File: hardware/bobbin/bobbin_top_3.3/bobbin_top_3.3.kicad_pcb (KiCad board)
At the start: 2 copper layers, 68.5 x 8.5 mm, 1 part

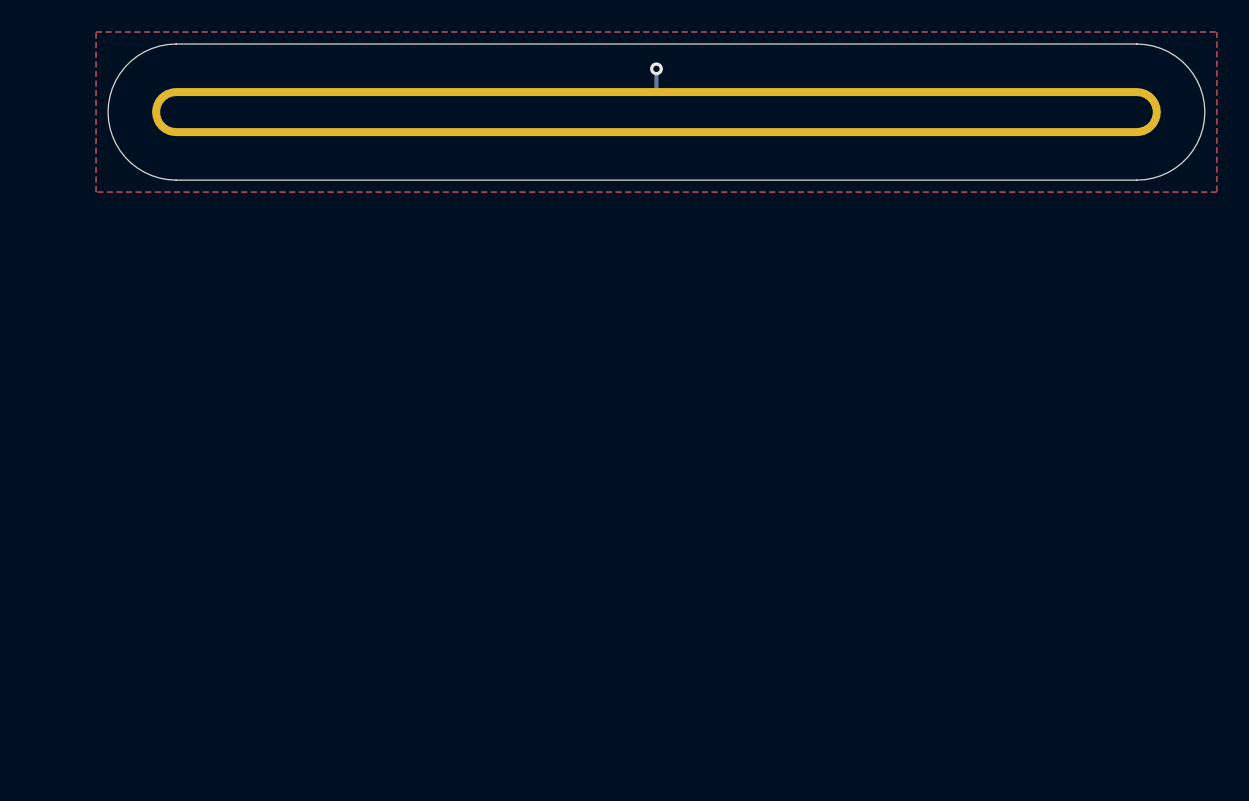
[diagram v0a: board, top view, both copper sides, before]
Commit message: Copied over bobbin_bottom to bobbin_top
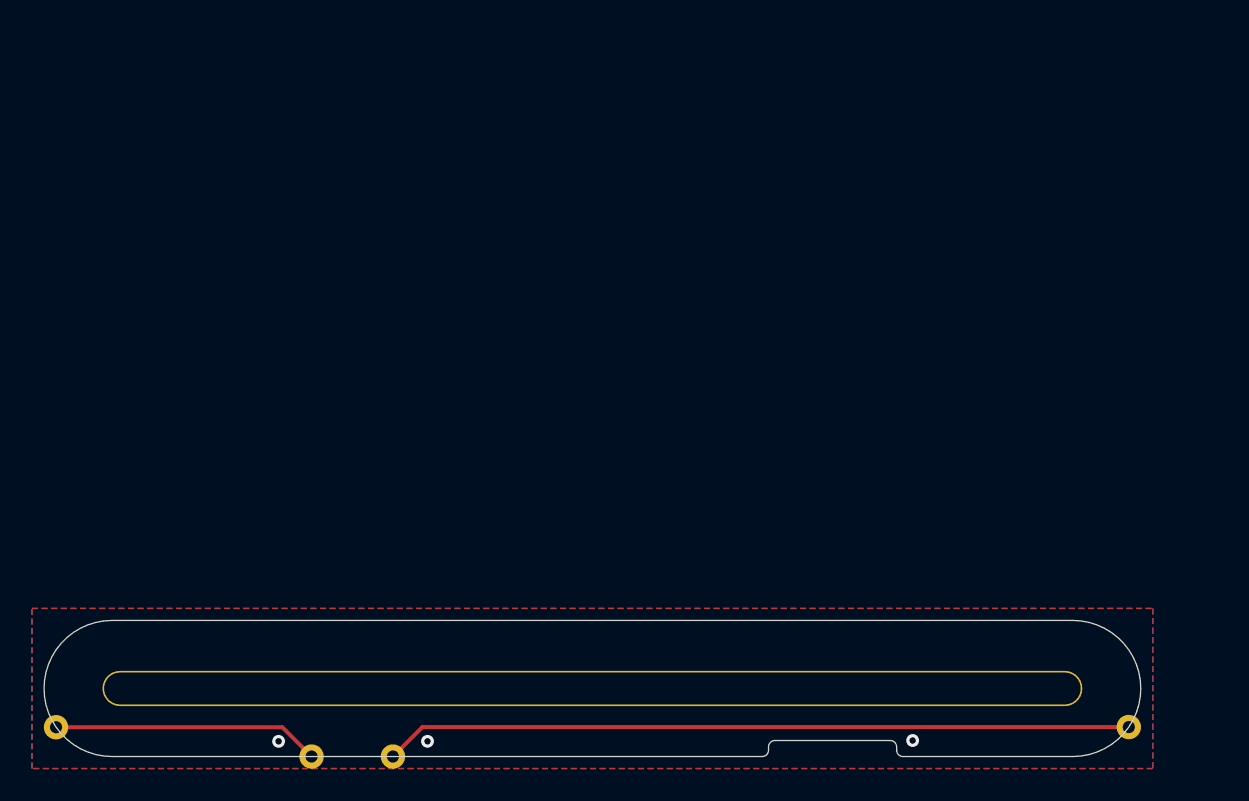
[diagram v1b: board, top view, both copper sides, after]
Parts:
- removed H3: ground-pad, cycfi_library:xr2-3.3-bobbin-top
- added H1: single_pad, xr_spectra_library:rail_slot_3.3, F.Cu at (130.0, 101.0)
- added J1: OC, cycfi_library:single-pad-1.52x1.52-th, F.Cu at (117.5, 105.2)
- added J2: OC, cycfi_library:single-pad-1.52x1.52-th, F.Cu at (163.5, 103.4)
- added J3: IC, cycfi_library:single-pad-1.52x1.52-th, F.Cu at (96.5, 103.4)
- added J4: IC, cycfi_library:single-pad-1.52x1.52-th, F.Cu at (112.5, 105.2)
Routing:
- net /OC: track 0.00 -> 46.7 mm
- net /IC: track 0.00 -> 16.7 mm
- net GND: track 2.70 -> 0.00 mm, vias 1 -> 3
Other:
- outline, holes or cut-outs redrawn
- net class Default removed

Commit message: Bobbin-top done
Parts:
- removed J1, J2: OC, cycfi_library:single-pad-1.52x1.52-th
- removed J3, J4: IC, cycfi_library:single-pad-1.52x1.52-th
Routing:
- net /OC: track 46.7 -> 0.00 mm
- net /IC: track 16.7 -> 0.00 mm
- net GND: vias 3 -> 0
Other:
- outline, holes or cut-outs redrawn
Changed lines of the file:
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@@
   (net 0 "")
   (net 1 "GND")
-  (net 2 "/OC")
-  (net 3 "/IC")
-  (footprint "cycfi_library:single-pad-1.52x1.52-th" (layer "F.Cu")
-    (at 117.54 105.25 180)
-    (property "Sheetfile" "bobbin_bottom_3.3.kicad_sch")
-    (property "Sheetname" "")
-    (attr through_hole)
-    (fp_text reference "J1" (at 0 2.54 180) (layer "F.SilkS") hide
-      (effects (font (size 1 1) (thickness 0.15)))
-    )
-    (fp_text value "OC" (at 0 -2.54 180) (layer "F.Fab")
-      (effects (font (size 1 1) (thickness 0.15)))
-    )
-    (pad "1" thru_hole circle (at 0 0 180) (size 1.52 1.52) (drill 0.76) (layers *.Cu *.Mask)
-      (net 2 "/OC") (pinfunction "Pin_1") (pintype "passive"))
-  )
-  (footprint "cycfi_library:single-pad-1.52x1.52-th" (layer "F.Cu")
-    (at 163.5 103.41 180)
-    (property "Sheetfile" "bobbin_bottom_3.3.kicad_sch")
-    (property "Sheetname" "")
-    (attr through_hole)
-    (fp_text reference "J2" (at 0 2.54) (layer "F.SilkS") hide
-      (effects (font (size 1 1) (thickness 0.15)))
-    )
-    (fp_text value "OC" (at -3 -0.09) (layer "F.Fab")
-      (effects (font (size 1 1) (thickness 0.15)))
-    )
-    (pad "1" thru_hole circle (at 0 0 180) (size 1.52 1.52) (drill 0.76) (layers *.Cu *.Mask)
-      (net 2 "/OC") (pinfunction "Pin_1") (pintype "passive"))
-  )
-  (footprint "cycfi_library:single-pad-1.52x1.52-th" (layer "F.Cu")
-    (at 96.5 103.42)
-    (property "Sheetfile" "bobbin_bottom_3.3.kicad_sch")
-    (property "Sheetname" "")
-    (attr through_hole)
-    (fp_text reference "J3" (at 0 2.54) (layer "F.SilkS") hide
-      (effects (font (size 1 1) (thickness 0.15)))
-    )
-    (fp_text value "IC" (at -2.75 0.08) (layer "F.Fab")
-      (effects (font (size 1 1) (thickness 0.15)))
-    )
-    (pad "1" thru_hole circle (at 0 0) (size 1.52 1.52) (drill 0.76) (layers *.Cu *.Mask)
-      (net 3 "/IC") (pinfunction "Pin_1") (pintype "passive"))
-  )
   (footprint "xr_spectra_library:rail_slot_3.3" (layer "F.Cu")
     (at 130 101)
-    (property "Sheetfile" "bobbin_bottom_3.3.kicad_sch")
+    (property "Sheetfile" "bobbin_top_3.3.kicad_sch")
     (property "Sheetname" "")
     (attr through_hole)
@@
     (pad "1" thru_hole oval (at 0 0) (size 61.2 2.2) (drill oval 61 2) (layers *.Cu *.Mask)
       (net 1 "GND") (pinfunction "1") (pintype "input"))
-  )
-  (footprint "cycfi_library:single-pad-1.52x1.52-th" (layer "F.Cu")
-    (at 112.46 105.25)
-    (property "Sheetfile" "bobbin_bottom_3.3.kicad_sch")
-    (property "Sheetname" "")
-    (attr through_hole)
-    (fp_text reference "J4" (at 0 2.54) (layer "F.SilkS") hide
-      (effects (font (size 1 1) (thickness 0.15)))
-    )
-    (fp_text value "IC" (at 0 2.25) (layer "F.Fab")
-      (effects (font (size 1 1) (thickness 0.15)))
-    )
-    (pad "1" thru_hole circle (at 0 0) (size 1.52 1.52) (drill 0.76) (layers *.Cu *.Mask)
-      (net 3 "/IC") (pinfunction "Pin_1") (pintype "passive"))
   )
   (gr_arc (start 149.4 105.25) (mid 149.117157 105.132843) (end 149 104.85) (layer "Dwgs.User") (width 0.01))
@@
   (gr_arc (start 100 105.25) (mid 95.75 101) (end 100 96.75) (layer "Dwgs.User") (width 0.01))
   (gr_line (start 141.4 104.25) (end 148.6 104.25) (layer "Dwgs.User") (width 0.01))
-  (gr_arc (start 148.6 104.25) (mid 148.882843 104.367157) (end 149 104.65) (layer "Edge.Cuts") (width 0.01))
-  (gr_line (start 141 104.85) (end 141 104.65) (layer "Edge.Cuts") (width 0.01))
-  (gr_line (start 149 104.65) (end 149 104.85) (layer "Edge.Cuts") (width 0.01))
-  (gr_arc (start 141 104.85) (mid 140.882843 105.132843) (end 140.6 105.25) (layer "Edge.Cuts") (width 0.01))
-  (gr_arc (start 141 104.65) (mid 141.117157 104.367157) (end 141.4 104.25) (layer "Edge.Cuts") (width 0.01))
   (gr_line (start 100 96.75) (end 160 96.75) (layer "Edge.Cuts") (width 0.01))
   (gr_arc (start 100 105.25) (mid 95.75 101) (end 100 96.75) (layer "Edge.Cuts") (width 0.01))
-  (gr_line (start 141.4 104.25) (end 148.6 104.25) (layer "Edge.Cuts") (width 0.01))
-  (gr_arc (start 149.4 105.25) (mid 149.117157 105.132843) (end 149 104.85) (layer "Edge.Cuts") (width 0.01))
-  (gr_line (start 140.6 105.25) (end 100 105.25) (layer "Edge.Cuts") (width 0.01))
-  (gr_line (start 160 105.25) (end 149.4 105.25) (layer "Edge.Cuts") (width 0.01))
+  (gr_line (start 160 105.25) (end 100 105.25) (layer "Edge.Cuts") (width 0.01))
   (gr_arc (start 160 96.75) (mid 164.25 101) (end 160 105.25) (layer "Edge.Cuts") (width 0.01))
-  (via (at 110.4 104.3) (size 0.8) (drill 0.4) (layers "F.Cu" "B.Cu") (free) (net 1))
-  (via (at 150 104.25) (size 0.8) (drill 0.4) (layers "F.Cu" "B.Cu") (free) (net 1))
-  (via (at 119.7 104.3) (size 0.8) (drill 0.4) (layers "F.Cu" "B.Cu") (free) (net 1))
-  (segment (start 119.38 103.41) (end 117.54 105.25) (width 0.25) (layer "F.Cu") (net 2))
-  (segment (start 163.5 103.41) (end 119.38 103.41) (width 0.25) (layer "F.Cu") (net 2))
-  (segment (start 96.5 103.42) (end 110.63 103.42) (width 0.25) (layer "F.Cu") (net 3))
-  (segment (start 110.63 103.42) (end 112.46 105.25) (width 0.25) (layer "F.Cu") (net 3))
   (zone (net 1) (net_name "GND") (layer "F.Cu") (hatch edge 0.508)
     (connect_pads (clearance 0.25))
